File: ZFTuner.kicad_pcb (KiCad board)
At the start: 4 copper layers, 221 x 82 mm, 164 parts, among them J101 RF_In, J102 RF_Out, J103 Tuner, J104 CAN, J201 SWD, J202 USB_C_Receptacle_USB2.0_16P, K401 HF3F-L-12-1ZL2T, K402 HF3F-L-12-1ZL2T, K403 HF3F-L-12-1ZL2T, K404 HF3F-L-12-1ZL2T, K405 HF3F-L-12-1ZL2T, K406 HF3F-L-12-1ZL2T, K407 HF3F-L-12-1ZL2T, K408 HF3F-L-12-1ZL2T, K501 HF3F-L-12-1ZL2T, K502 HF3F-L-12-1ZL2T, K503 HF3F-L-12-1ZL2T, K504 HF3F-L-12-1ZL2T, K505 HF3F-L-12-1ZL2T, K506 HF3F-L-12-1ZL2T, K507 HF3F-L-12-1ZL2T, Q401 AO3401A, Q402 AO3401A, Q403 AO3400, Q404 AO3400, Q501 AO3401A, Q502 AO3401A, Q503 AO3400, Q504 AO3400, Q601 AO3401A, SW201 CL-SB_22A-12T, U201 ULN2803A, U202 IP4234CZ6, U203 STM32G431CBTx, U204 MCP2542FDxMF, U205 ILD74, U301 LTC5507, U302 LTC5507, U601 HT7463A, U602 BD2243G, U603 MIC5504-3.3YM5, Y201 24MHz

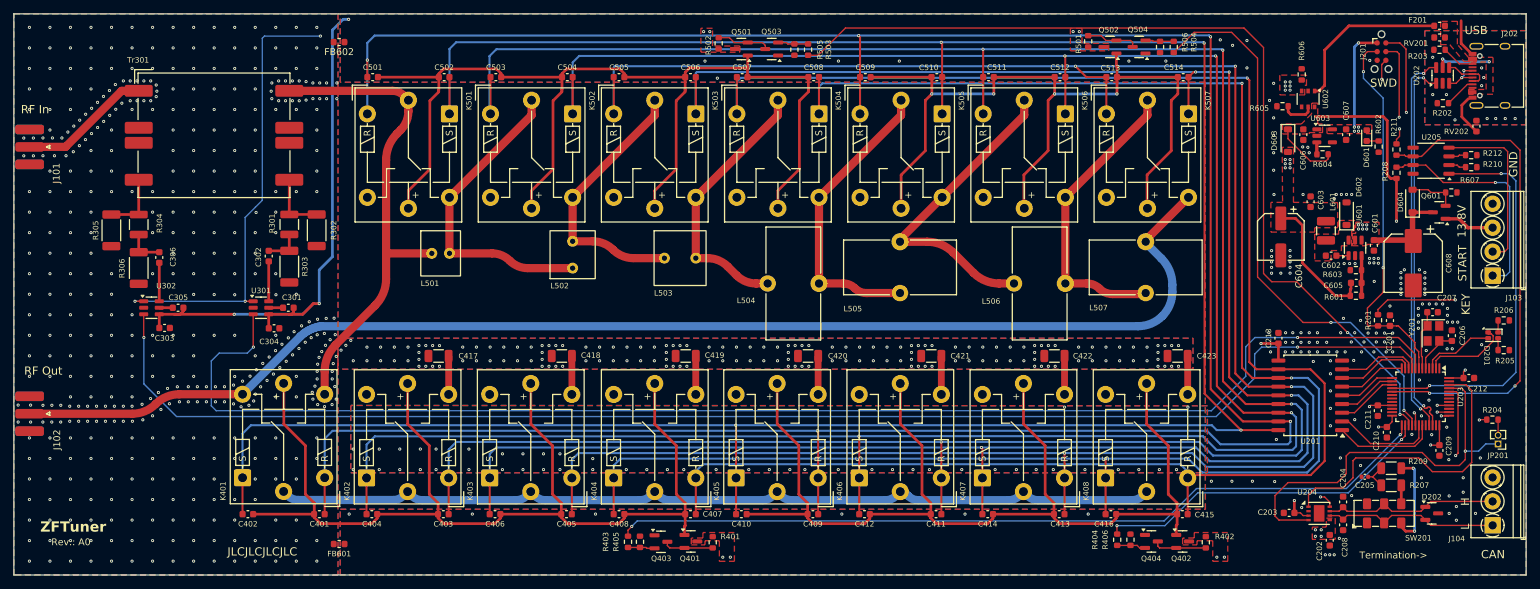
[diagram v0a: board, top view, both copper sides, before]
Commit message: Re-stiched GNDD vias. Added mounting holes.
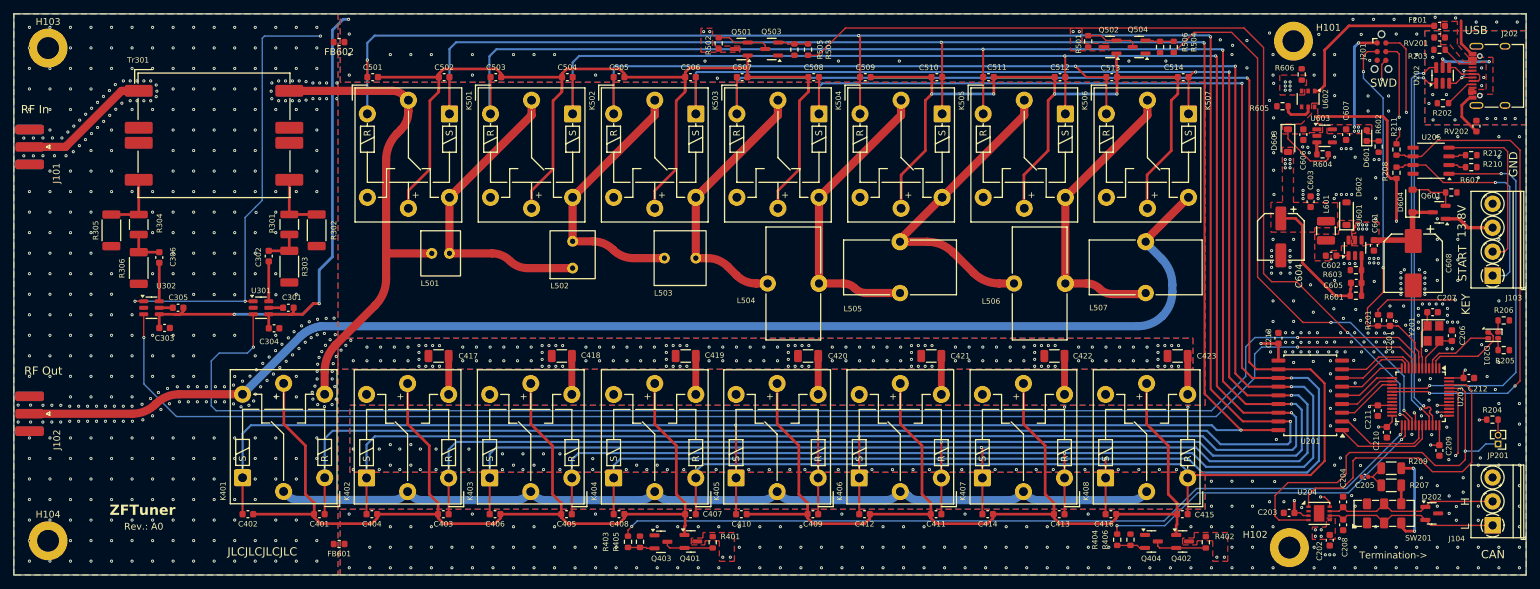
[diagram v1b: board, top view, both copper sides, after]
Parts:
- added H101: Right_Up, MountingHole:MountingHole_3.2mm_M3_ISO7380_Pad, F.Cu at (231.0, 44.5)
- added H102: Right_Down, MountingHole:MountingHole_3.2mm_M3_ISO7380_Pad, F.Cu at (230.4, 118.5)
- added H103: Left_up, MountingHole:MountingHole_3.2mm_M3_ISO7380_Pad, F.Cu at (49.0, 45.5)
- added H104: Left_Down, MountingHole:MountingHole_3.2mm_M3_ISO7380_Pad, F.Cu at (49.0, 117.5)
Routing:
- net GNDPWR: vias 11 -> 13
- net GNDD: vias 207 -> 457

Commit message: Minor layout improvements
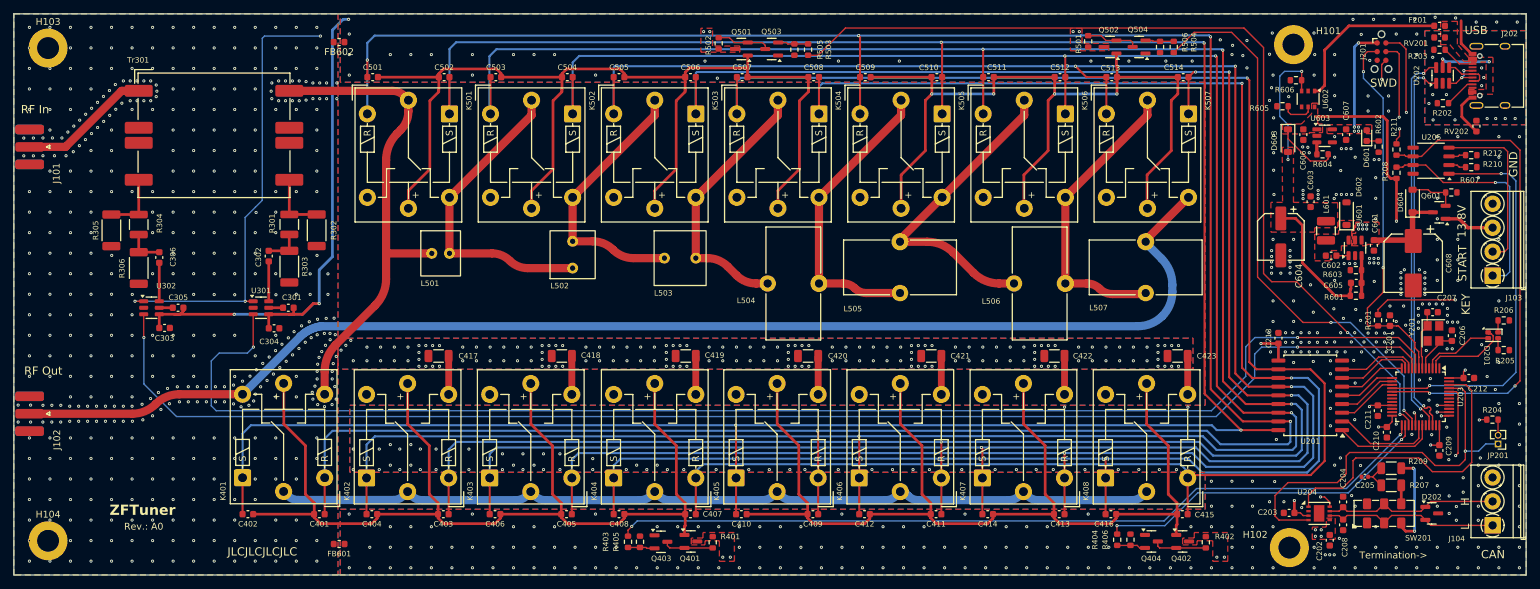
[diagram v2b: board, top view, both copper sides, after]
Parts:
- moved R606 1.19 mm to (231.4, 50.2), turned to 0 degrees
- moved H101 0.50 mm to (231.0, 45.0)
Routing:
- net +5.4V: track 20.0 -> 39.0 mm, vias 12 -> 2
- net GNDD: vias 457 -> 463
- net GND: vias 615 -> 623
- removed copper zone on In2.Cu, net +5.4V

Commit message: Finished layout
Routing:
- net GNDPWR: vias 13 -> 15
- net GNDD: vias 463 -> 561
- net GND: vias 623 -> 625

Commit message: Fixed directional couler footprint. Improved RF In/Out SMA placement.
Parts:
- moved J102 3.56 mm to (46.4, 102.5)
- moved J101 0.55 mm to (46.3, 60.5)
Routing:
- net /RF_Out: track 192.3 -> 193.6 mm
- net Net-(Tr301-Reverse): track 9.06 -> 10.1 mm
- net GND: vias 625 -> 258
